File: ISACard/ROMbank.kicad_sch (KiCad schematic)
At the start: 19 parts, among them U10 28C256, U6 74LS86, U7 74LS86, U8 74LS32, U9 74LS32

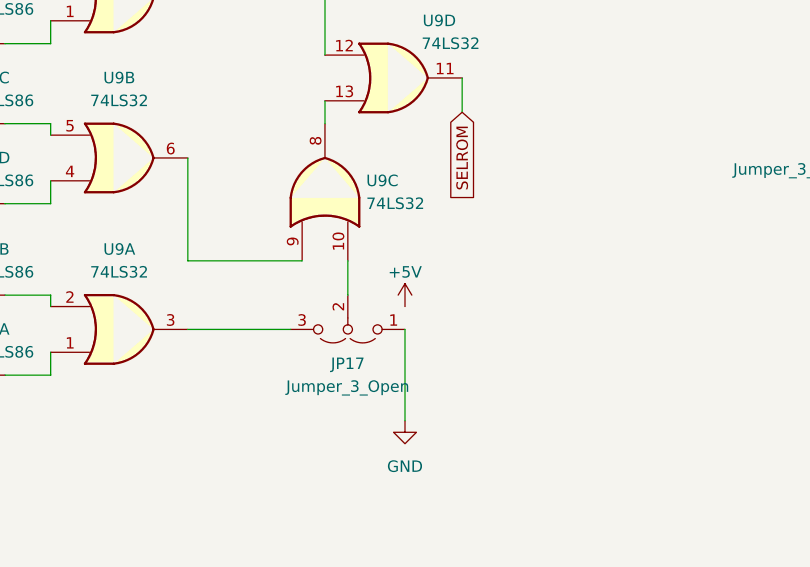
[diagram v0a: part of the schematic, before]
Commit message: Added gerber files and CS/CS2 to feature connector
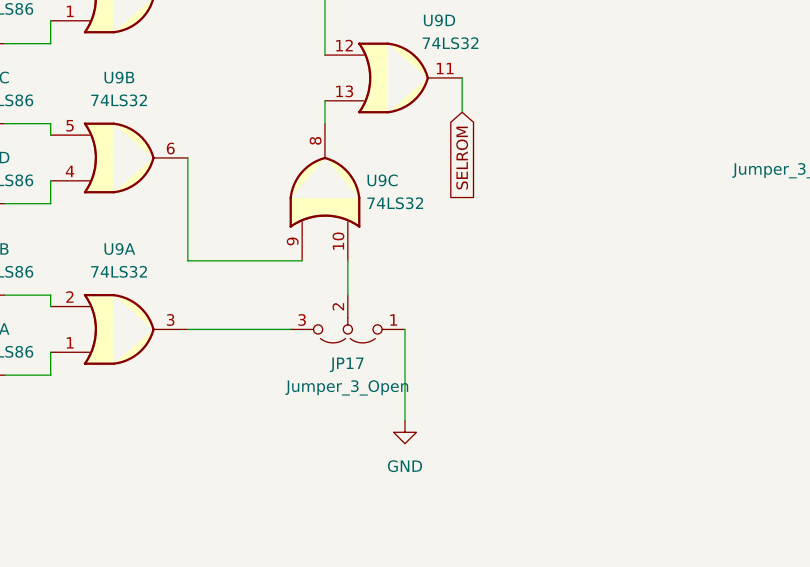
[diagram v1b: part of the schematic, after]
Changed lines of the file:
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@@
-    (pin "1")
-  )
-  (symbol (lib_id "power:+5V") (at 162.56 129.54 0) (unit 1)
-    (in_bom yes) (on_board yes)
-    (property "Reference" "#PWR0121" (id 0) (at 162.56 133.35 0)
-      (effects (font (size 1.27 1.27)) hide)
-    )
-    (property "Value" "+5V" (id 1) (at 162.56 125.73 0))
-    (property "Footprint" "" (id 2) (at 162.56 129.54 0)
-      (effects (font (size 1.27 1.27)) hide)
-    )
-    (property "Datasheet" "" (id 3) (at 162.56 129.54 0)
-      (effects (font (size 1.27 1.27)) hide)
-    )
     (pin "1")
   )

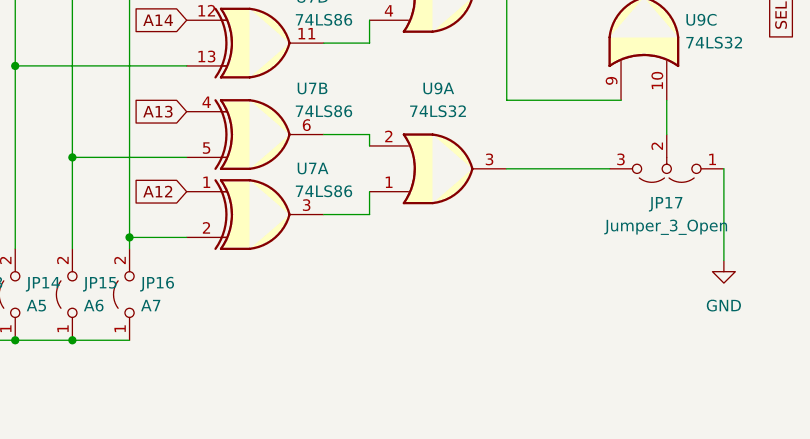
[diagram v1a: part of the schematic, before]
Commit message: Added 16k/32k jumper
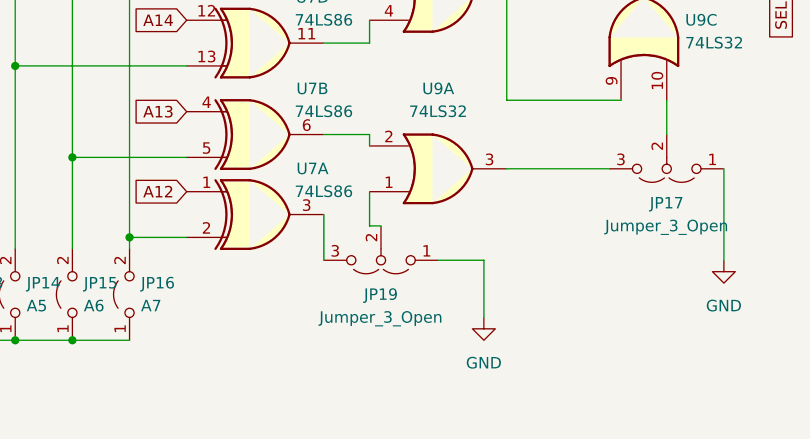
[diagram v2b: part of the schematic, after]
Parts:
- added JP19: Jumper_3_Open, Connector_PinHeader_2.54mm:PinHeader_1x03_P2.54mm_Vertical, symbol Jumper:Jumper_3_Open
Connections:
- net GND: now also JP19.1 (A)
- net at U9.1: now also JP19.2 (C); no longer U7.3
- new net: JP19.3 (B), U7.3
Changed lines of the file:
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@@
+    (stroke (width 0) (type default) (color 0 0 0 0))
+  )
+  (wire (pts (xy 123.19 138.43) (xy 123.19 134.62))
     (stroke (width 0) (type default) (color 0 0 0 0))
   )
@@
     (stroke (width 0) (type default) (color 0 0 0 0))
   )
-  (wire (pts (xy 123.19 134.62) (xy 123.19 137.16))
+  (wire (pts (xy 118.11 137.16) (xy 118.11 142.24))
     (stroke (width 0) (type default) (color 0 0 0 0))
   )
@@
     (stroke (width 0) (type default) (color 0 0 0 0))
   )
-  (wire (pts (xy 123.19 137.16) (xy 118.11 137.16))
-    (stroke (width 0) (type default) (color 0 0 0 0))
-  )
   (wire (pts (xy 83.82 60.96) (xy 90.17 60.96))
     (stroke (width 0) (type default) (color 0 0 0 0))
@@
     (stroke (width 0) (type default) (color 0 0 0 0))
   )
+  (wire (pts (xy 135.89 142.24) (xy 130.81 142.24))
+    (stroke (width 0) (type default) (color 0 0 0 0))
+  )
   (wire (pts (xy 64.77 93.98) (xy 102.87 93.98))
     (stroke (width 0) (type default) (color 0 0 0 0))
   )
+  (wire (pts (xy 135.89 148.59) (xy 135.89 142.24))
+    (stroke (width 0) (type default) (color 0 0 0 0))
+  )
   (wire (pts (xy 96.52 139.7) (xy 102.87 139.7))
     (stroke (width 0) (type default) (color 0 0 0 0))
@@
   )
   (wire (pts (xy 231.14 74.93) (xy 233.68 74.93))
+    (stroke (width 0) (type default) (color 0 0 0 0))
+  )
+  (wire (pts (xy 124.46 138.43) (xy 123.19 138.43))
     (stroke (width 0) (type default) (color 0 0 0 0))
   )
@@
     (pin "1")
     (pin "2")
+  )
+  (symbol (lib_id "Jumper:Jumper_3_Open") (at 124.46 142.24 180) (unit 1)
+    (in_bom yes) (on_board yes) (fields_autoplaced)
+    (property "Reference" "JP19" (id 0) (at 124.46 146.05 0))
+    (property "Value" "Jumper_3_Open" (id 1) (at 124.46 148.59 0))
+    (property "Footprint" "Connector_PinHeader_2.54mm:PinHeader_1x03_P2.54mm_Vertical" (id 2) (at 124.46 142.24 0)
+      (effects (font (size 1.27 1.27)) hide)
+    )
+    (property "Datasheet" "~" (id 3) (at 124.46 142.24 0)
+      (effects (font (size 1.27 1.27)) hide)
+    )
+    (pin "1")
+    (pin "2")
+    (pin "3")
   )
   (symbol (lib_id "Jumper:Jumper_2_Open") (at 64.77 146.05 90) (unit 1)
@@
       (effects (font (size 1.27 1.27)) hide)
     )
+    (pin "1")
+  )
+  (symbol (lib_id "power:GND") (at 135.89 148.59 0) (unit 1)
+    (in_bom yes) (on_board yes) (fields_autoplaced)
+    (property "Reference" "#PWR0121" (id 0) (at 135.89 154.94 0)
+      (effects (font (size 1.27 1.27)) hide)
+    )
+    (property "Value" "GND" (id 1) (at 135.89 153.67 0))
+    (property "Footprint" "" (id 2) (at 135.89 148.59 0)
+      (effects (font (size 1.27 1.27)) hide)
+    )
+    (property "Datasheet" "" (id 3) (at 135.89 148.59 0)
+      (effects (font (size 1.27 1.27)) hide)
+    )
